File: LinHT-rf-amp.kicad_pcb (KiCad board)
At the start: 4 copper layers, 35 x 20 mm, 24 parts, among them J1 INPUT, J2 OUTPUT, J4 SIGNALS, U1 GRF5604

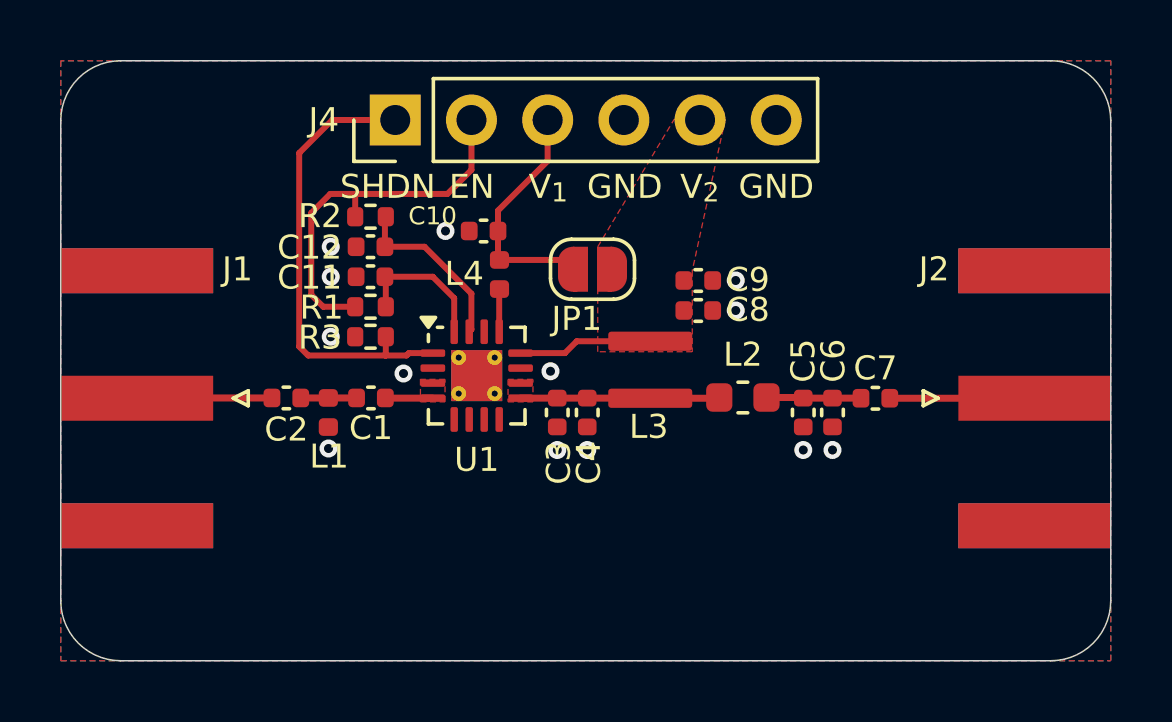
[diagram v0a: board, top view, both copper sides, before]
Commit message: Fixed RF traces, reset annotation, added M2 holes
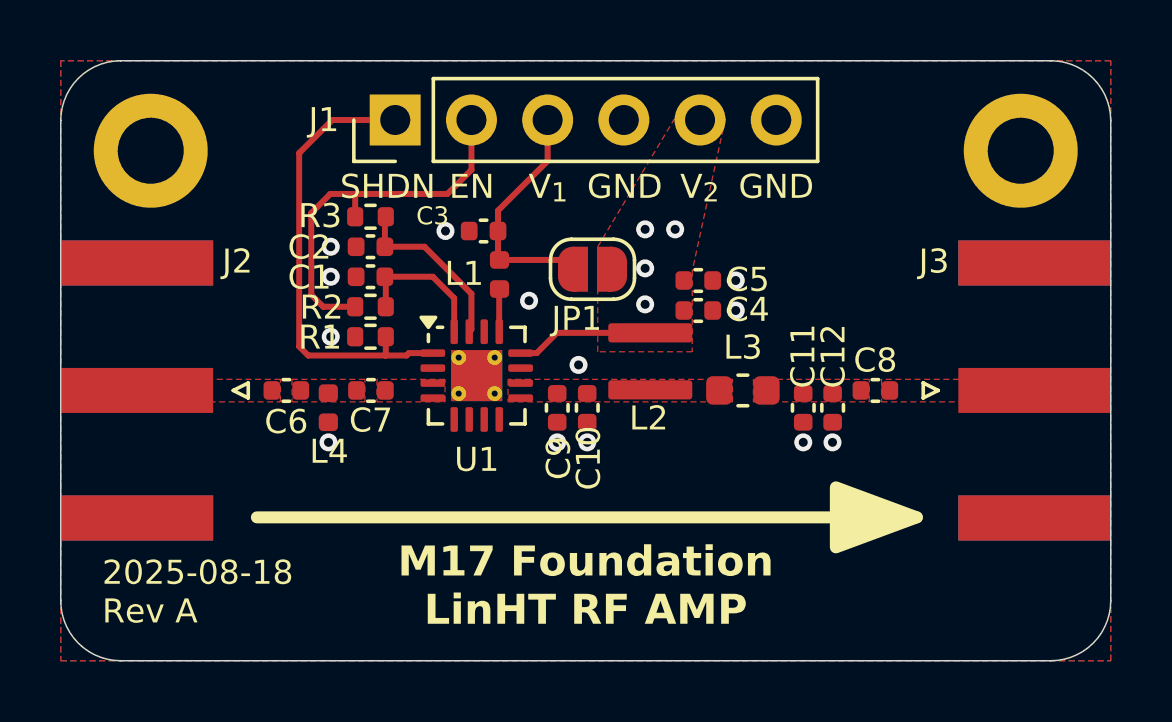
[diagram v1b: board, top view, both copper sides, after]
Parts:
- added H1: MountingHole_Pad_MP, MountingHole:MountingHole_2.2mm_M2_DIN965_Pad, F.Cu at (137.3, 88.9)
- added H2: MountingHole_Pad_MP, MountingHole:MountingHole_2.2mm_M2_DIN965_Pad, F.Cu at (166.3, 88.9)
- moved L2 0.28 mm to (154.0, 95.9)
- moved C8 0.26 mm to (161.5, 96.9)
- moved J2 0.26 mm to (136.9, 96.9)
- moved J3 0.26 mm to (166.8, 96.9)
- moved C6 0.25 mm to (141.9, 96.9)
- moved C7 0.25 mm to (144.7, 96.9)
- moved L3 0.23 mm to (157.1, 96.9)
- moved L4 0.16 mm to (143.3, 97.4)
- moved C12 0.16 mm to (160.1, 97.4)
- moved C10 0.16 mm to (151.9, 97.4)
- moved C11 0.16 mm to (159.1, 97.4)
- moved C9 0.16 mm to (150.9, 97.4)
- renumbered C11 to C1, C4 to C10, C5 to C11, C6 to C12, C12 to C2, C10 to C3, C8 to C4, C9 to C5, C2 to C6, C1 to C7, C7 to C8, C3 to C9, J4 to J1, J1 to J2, J2 to J3, L4 to L1, L3 to L2, L2 to L3, L1 to L4, R3 to R1, R1 to R2, R2 to R3
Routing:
- net Net-(C10-Pad2): track 6.63 -> 0.00 mm
- net Net-(J3-In): track 4.82 -> 0.00 mm
- net Net-(J2-In): track 4.50 -> 0.00 mm
- net Net-(C11-Pad2): track 3.16 -> 0.00 mm
- net Net-(C6-Pad2): track 1.86 -> 0.00 mm
- net Net-(C7-Pad2): track 1.58 -> 0.00 mm
- net /V_{2}: track 4.49 -> 4.60 mm, vias 0 -> 4
- added copper zone on In2.Cu, net /V_{2}
- added copper zone on In1.Cu, net GND
- added copper zone on F.Cu, net Net-(C11-Pad2)
- added copper zone on F.Cu, net Net-(C6-Pad2)
- added copper zone on F.Cu, net Net-(J2-In)
- added copper zone on F.Cu, net Net-(J3-In)
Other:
- board text added: "${ISSUE_DATE} Rev ${REVISION}"
- board text added: "LinHT 390-470 MHz Power Amplifier GRF5604 6 Watt"
- board text added: "M17 Foundation LinHT RF AMP"
- board text added: "Vlastimil OK5VAS Wojciech SP5WWP Andreas OE3ANC"

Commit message: Added more vias and via fencing around RF traces
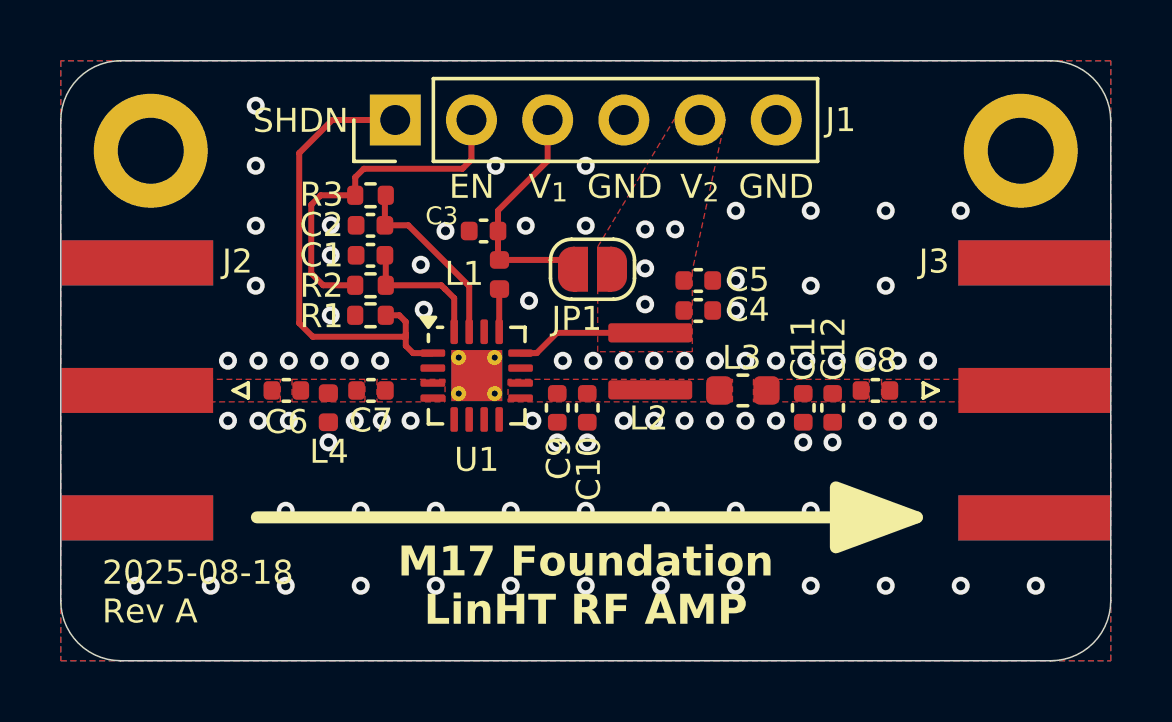
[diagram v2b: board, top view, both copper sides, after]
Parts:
- moved C1 0.72 mm to (144.7, 92.4)
- moved C2 0.72 mm to (144.7, 91.4)
- moved R1 0.72 mm to (144.7, 94.4)
- moved R2 0.72 mm to (144.7, 93.4)
- moved R3 0.72 mm to (144.7, 90.4)
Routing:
- net /ENABLE: track 12.7 -> 11.6 mm
- net GND: vias 13 -> 85
